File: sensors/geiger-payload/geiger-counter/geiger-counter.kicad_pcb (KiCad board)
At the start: 2 copper layers, 121.3 x 46.1 mm, 38 parts, among them J1 3531, J2 3531, J4 Conn_02x03_Odd_Even, J5 Conn_01x06, J6 Conn_01x03, Q1 MMBTA44, Q2 MMBT3904, Q3 MMBT3904, SW1 SW_Push, SW2 SW_SPDT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

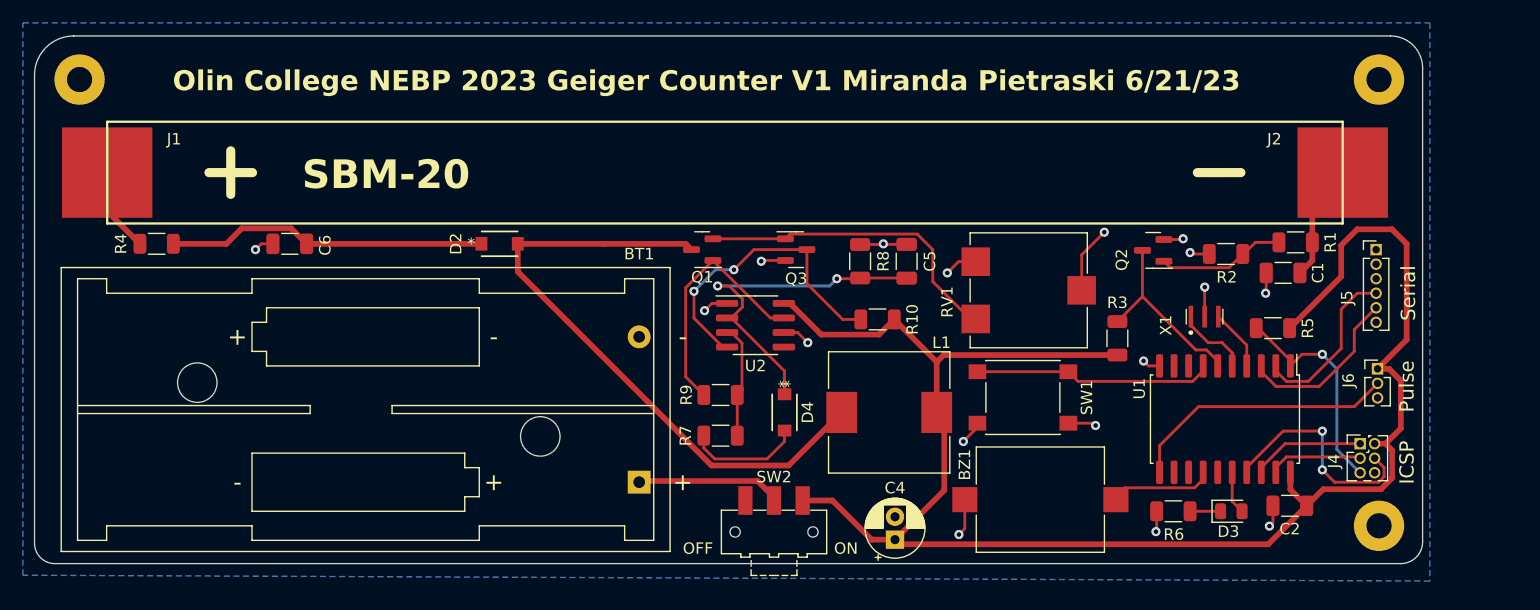
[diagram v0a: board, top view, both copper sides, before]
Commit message: pcb alterations due to part sourcing
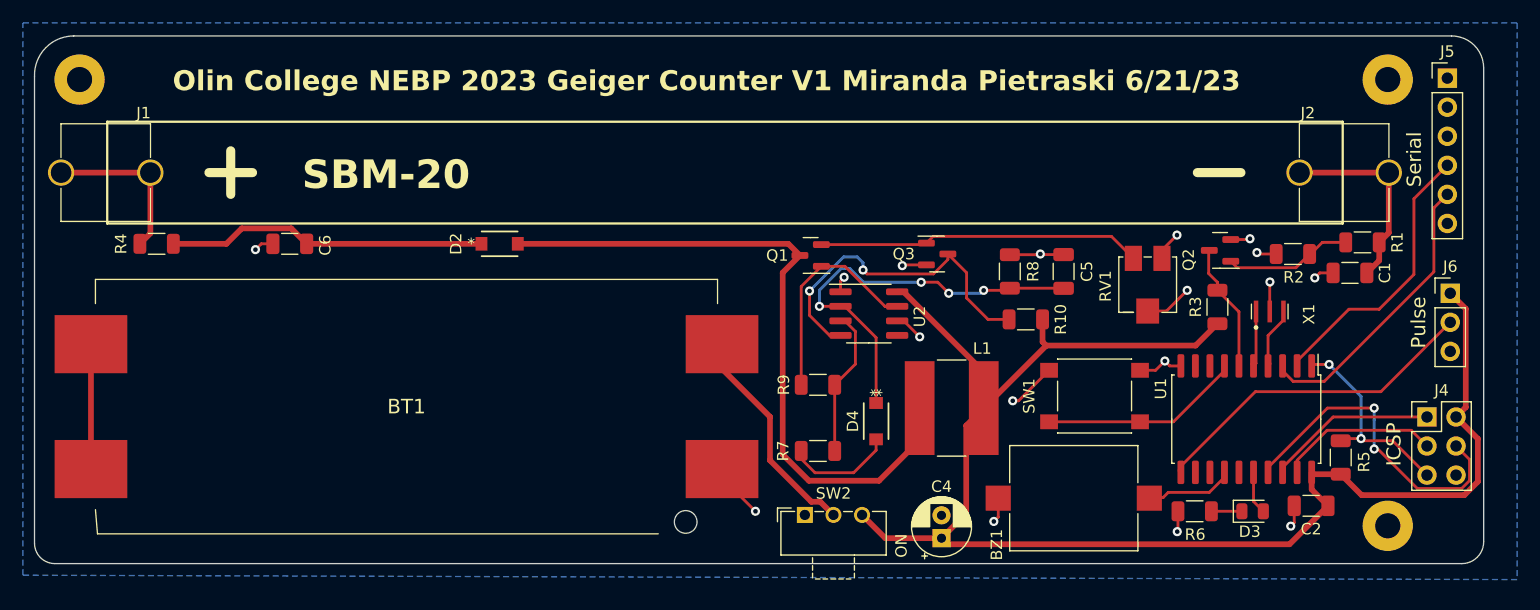
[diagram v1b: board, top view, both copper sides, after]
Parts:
- BT1: value 3V -> ~; footprint Battery:BatteryHolder_Keystone_2468_2xAAA -> Geiger Footprints:1022
- J1, J2: value 3531 -> ~; footprint Geiger Footprints:FUSE_3531 -> Geiger Footprints:FUSE_3514
- J4: footprint Connector_PinHeader_1.27mm:PinHeader_2x03_P1.27mm_Vertical -> Connector_PinHeader_2.54mm:PinHeader_2x03_P2.54mm_Vertical
- J5: footprint Connector_PinHeader_1.27mm:PinHeader_1x06_P1.27mm_Vertical -> Connector_PinHeader_2.54mm:PinHeader_1x06_P2.54mm_Vertical
- J6: footprint Connector_PinHeader_1.27mm:PinHeader_1x03_P1.27mm_Vertical -> Connector_PinHeader_2.54mm:PinHeader_1x03_P2.54mm_Vertical
- L1: footprint Inductor_SMD:L_10.4x10.4_H4.8 -> Inductor_SMD:L_Bourns-SRN8040_8x8.15mm
- RV1: footprint Potentiometer_SMD:Potentiometer_ACP_CA9-VSMD_Vertical -> Geiger Footprints:G43A
- SW2: footprint Button_Switch_SMD:SW_SPDT_CK-JS102011SAQN -> Geiger Footprints:TP-33103
- moved BT1 21.4 mm to (121.4, 55.4)
- moved J5 16.2 mm to (212.3, 26.7)
- moved C5 13.7 mm to (178.8, 43.6)
- moved R8 13.1 mm to (174.1, 43.6)
- moved R10 13.0 mm to (175.5, 47.8)
- moved R5 12.8 mm to (203.0, 59.8), turned to 90 degrees
- moved Q3 12.3 mm to (167.8, 42.0)
- moved RV1 10.4 mm to (186.2, 44.7), turned to 90 degrees
- moved U2 9.96 mm to (161.8, 47.2)
- moved Q1 9.49 mm to (156.7, 42.2)
- moved J6 9.16 mm to (212.6, 45.5)
- moved R3 9.16 mm to (192.3, 46.7)
- moved R7 8.61 mm to (157.4, 59.2)
- moved R9 8.56 mm to (157.4, 53.5)
- moved D4 8.04 mm to (162.4, 56.6)
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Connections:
- BT1 pad 1: Net-(BT1-+) -> GND
- BT1 pad 2: GND -> Net-(BT1-+)
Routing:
- net VCC: track 149.8 -> 133.1 mm
- net Net-(BT1-Pad3): track 0.00 -> 10.9 mm
- net Net-(J5-Pin_5): track 15.0 -> 25.2 mm
- net Net-(J5-Pin_4): track 15.3 -> 25.4 mm
- net Net-(J4-Pin_4): track 19.7 -> 29.0 mm
- net Net-(C1-Pad1): track 10.4 -> 17.4 mm
- net Net-(J1-Pad1): track 7.41 -> 14.4 mm
- net Net-(BT1-+): track 12.7 -> 19.4 mm
- net Net-(U2-TR): track 30.9 -> 37.0 mm, vias 2 -> 4
- net /GM_PULSE: track 17.4 -> 11.4 mm
- net Net-(J4-Pin_3): track 8.22 -> 14.1 mm
- net Net-(J6-Pin_2): track 23.9 -> 29.5 mm
- net Net-(Q1-C): track 55.1 -> 60.3 mm
- net Net-(J4-Pin_1): track 10.5 -> 14.9 mm
- net GND: track 42.8 -> 46.6 mm
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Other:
- board size 121.3 x 46.1 mm -> 126.6 x 46.1 mm
- board text removed: "OFF"

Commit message: pcb design changes
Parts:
- C1, C2, C5: footprint Capacitor_SMD:C_1206_3216Metric -> Capacitor_SMD:C_0805_2012Metric
- L1: footprint Inductor_SMD:L_Bourns-SRN8040_8x8.15mm -> Inductor_SMD:L_Changjiang_FNR6045S
- R1, R10, R2, R3, R5, R6, R7, R8, R9: footprint Resistor_SMD:R_1206_3216Metric -> Resistor_SMD:R_0805_2012Metric
- SW1: footprint Button_Switch_SMD:SW_Push_1P1T_NO_6x6mm_H9.5mm -> Button_Switch_SMD:SW_Push_1P1T_XKB_TS-1187A
- moved C5 6.14 mm to (174.0, 47.4), turned to 0 degrees
- moved R10 4.62 mm to (180.1, 47.1), turned to 90 degrees
- moved C4 2.56 mm to (168.4, 64.3), turned to -90 degrees
- moved U2 1.48 mm to (162.6, 48.5)
- moved SW1 1.18 mm to (180.3, 54.4)
- moved C1 1.16 mm to (203.6, 44.8)
- moved R7 1.09 mm to (157.5, 58.2)
- moved R2 1.07 mm to (198.2, 41.1)
- moved SW2 0.63 mm to (158.7, 68.9)
- moved C2 0.61 mm to (200.4, 64.6), turned to 0 degrees
- moved D2 0.60 mm to (130.1, 41.4)
- moved R4 0.60 mm to (100.1, 41.4)
- moved C6 0.60 mm to (111.7, 41.4)
- moved R8 0.10 mm to (174.0, 43.6), turned to 0 degrees
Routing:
- net VCC: track 133.1 -> 127.7 mm
- net GND: track 46.6 -> 41.4 mm, vias 17 -> 18
- net Net-(U2-TR): track 37.0 -> 32.1 mm, vias 4 -> 0
- net Net-(Q3-C): track 30.0 -> 34.8 mm, vias 2 -> 0
- net Net-(Q1-B): track 19.2 -> 23.2 mm, vias 0 -> 2
- net Net-(BT1-+): track 19.4 -> 21.7 mm
- net Net-(D4-Pad2): track 9.51 -> 7.64 mm
- net Net-(C1-Pad1): track 17.4 -> 18.8 mm
- net Net-(Q1-C): track 60.3 -> 61.6 mm
- net Net-(U2-Q): track 12.9 -> 11.6 mm
- net /GM_PULSE: track 11.4 -> 11.9 mm
- net Net-(D3-K): track 3.16 -> 3.71 mm
- net Net-(J4-Pin_5): track 18.9 -> 19.4 mm
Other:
- board text added: "Olin College NEBP 2023 Geiger Counter V1 Miranda Pietraski 6/26"
- board text removed: "Olin College NEBP 2023 Geiger Counter V1 Miranda Pietraski 6/21/23"
